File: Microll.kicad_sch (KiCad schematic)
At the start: 13 parts, among them J1 USB_C_Receptacle, U1 AP7173-FNG-7, U2 STM32G0B1CBU6, U3 ESP32-C3-WROOM-02-N4, U4 LSM6DSL

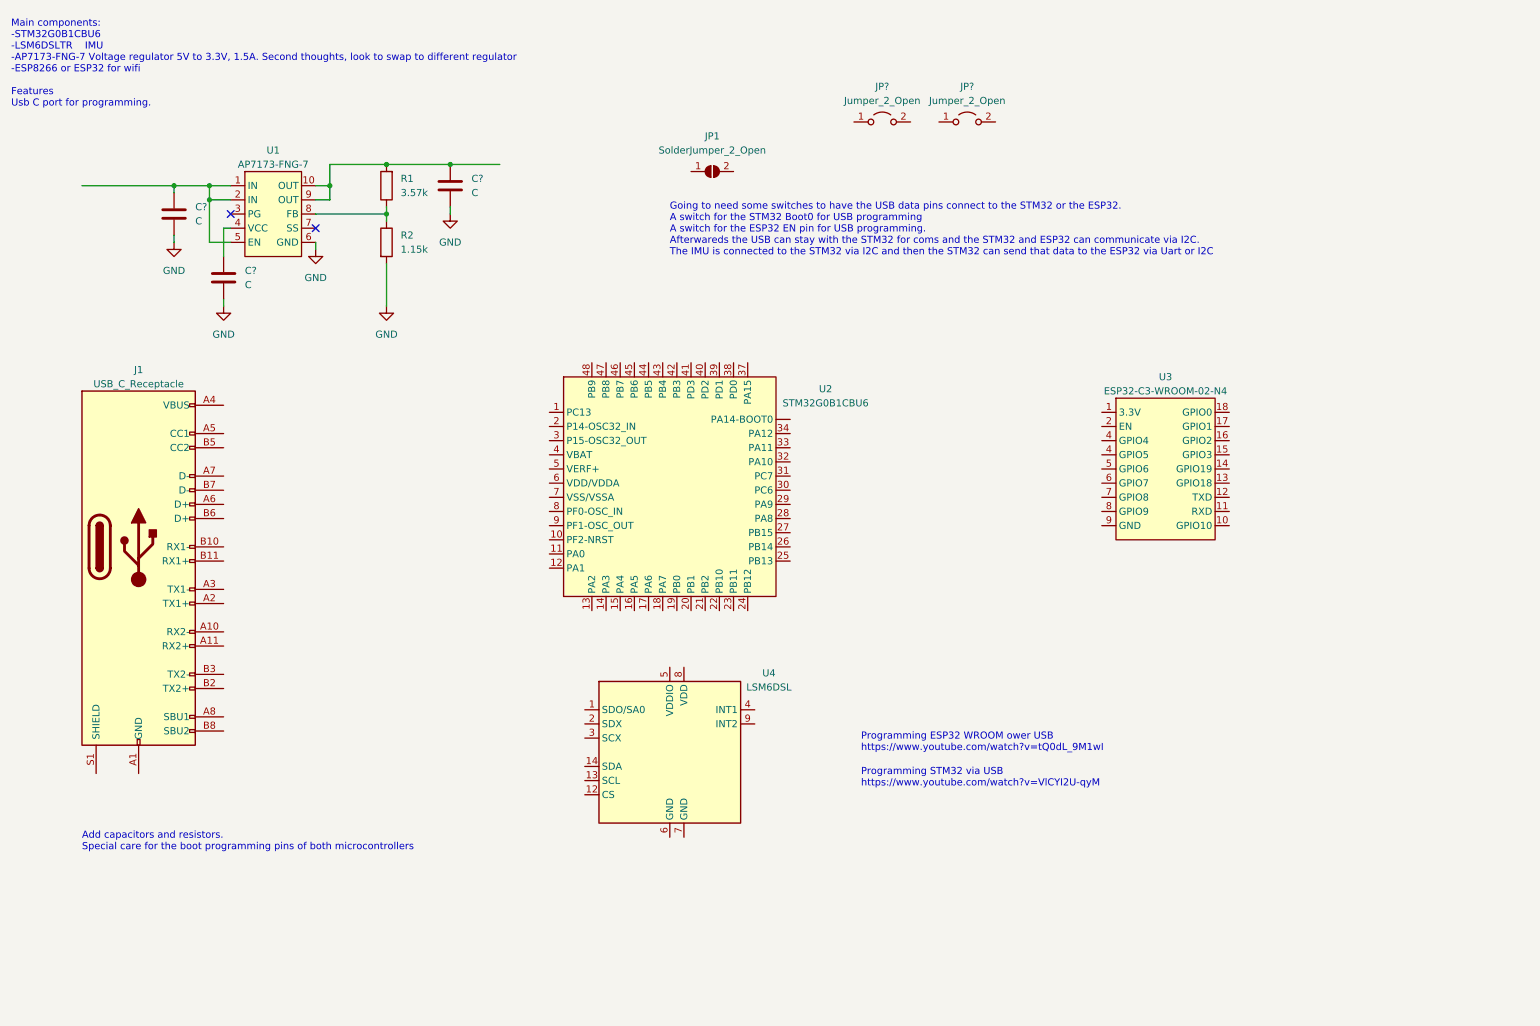
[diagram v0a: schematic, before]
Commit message: Changed linear regulator to TLV767
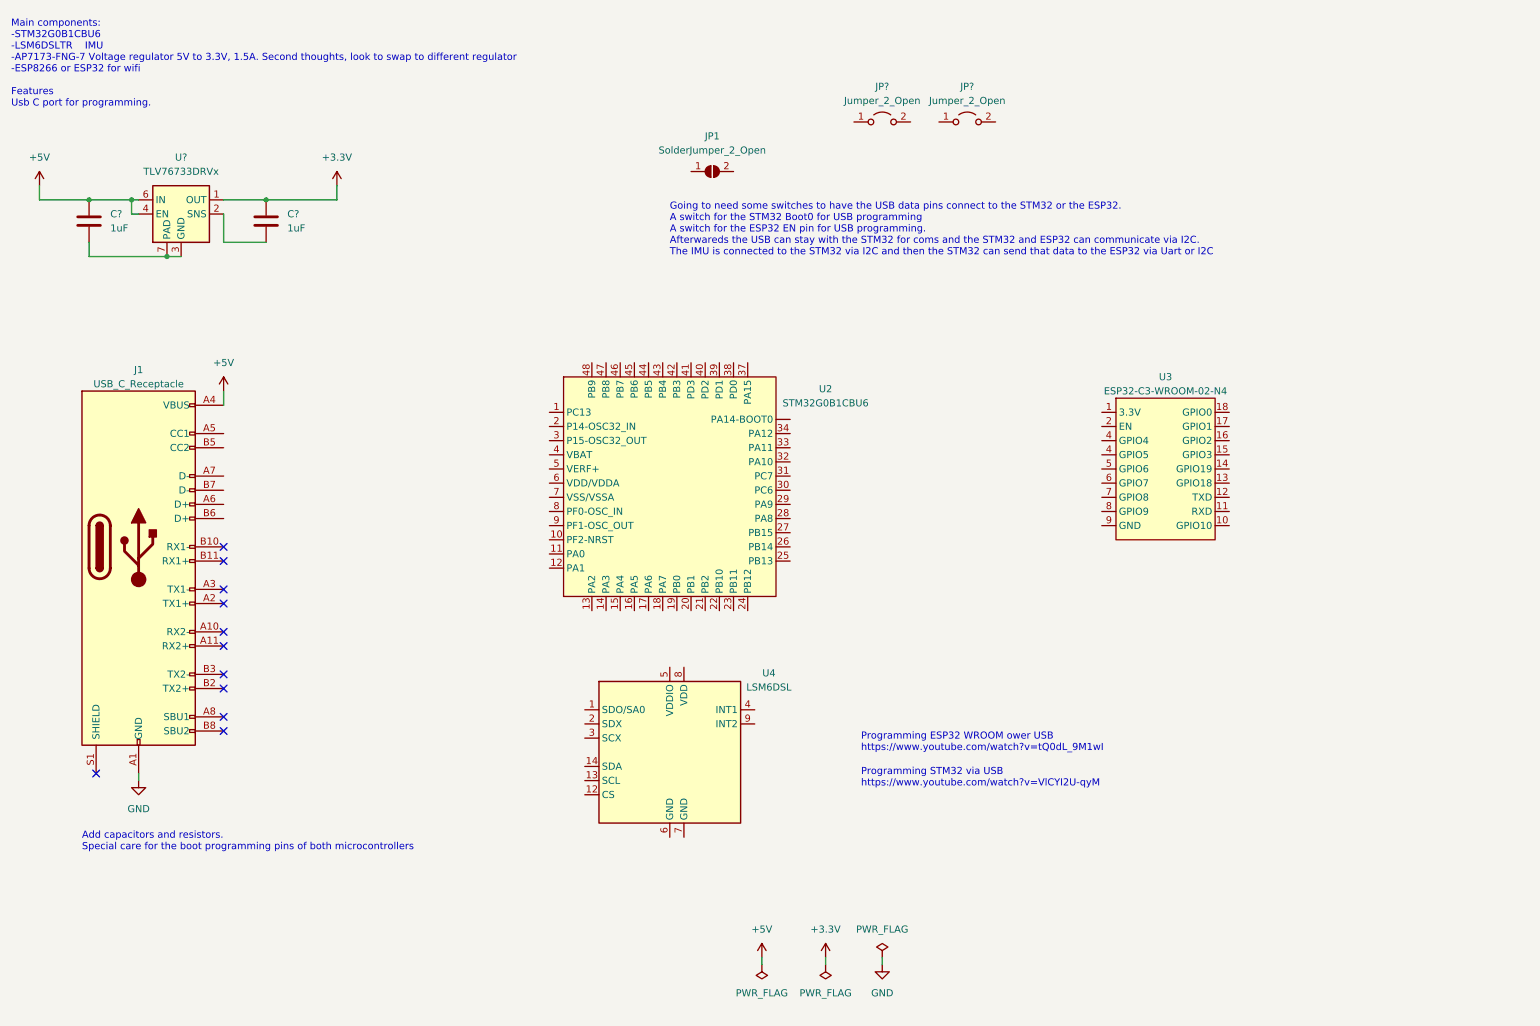
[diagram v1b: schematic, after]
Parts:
- removed C? (x3): C, symbol Device:C
- removed R1: 3.57k, symbol Device:R
- removed R2: 1.15k, symbol Device:R
- removed U1: AP7173-FNG-7, AP7173-FNG-7:AP7173-FNG-7, symbol AP7173-FNG-7:AP7173-FNG-7
- added C? (x2): 1uF, symbol Device:C
- added U?: TLV76733DRVx, Package_SON:WSON-6-1EP_2x2mm_P0.65mm_EP1x1.6mm_ThermalVias, symbol Regulator_Linear:TLV76733DRVx
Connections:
- net GND: now also J1.A1 (GND), J1.A12 (GND), J1.B1 (GND), J1.B12 (GND)
- net +5V: now reaches J1.A4 (VBUS), J1.A9 (VBUS), J1.B4 (VBUS), J1.B9 (VBUS)
- net +5V: now also C?.1, U?.4 (EN), U?.6 (IN)
- new net: C?.2, U?.2 (SNS)
- new net: C?.2, U?.3 (GND), U?.5 (GND), U?.7 (PAD)
- new net +3.3V: C?.1, U?.1 (OUT)
- no-connect marks 2 -> 11
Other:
- title: (none) -> Microll

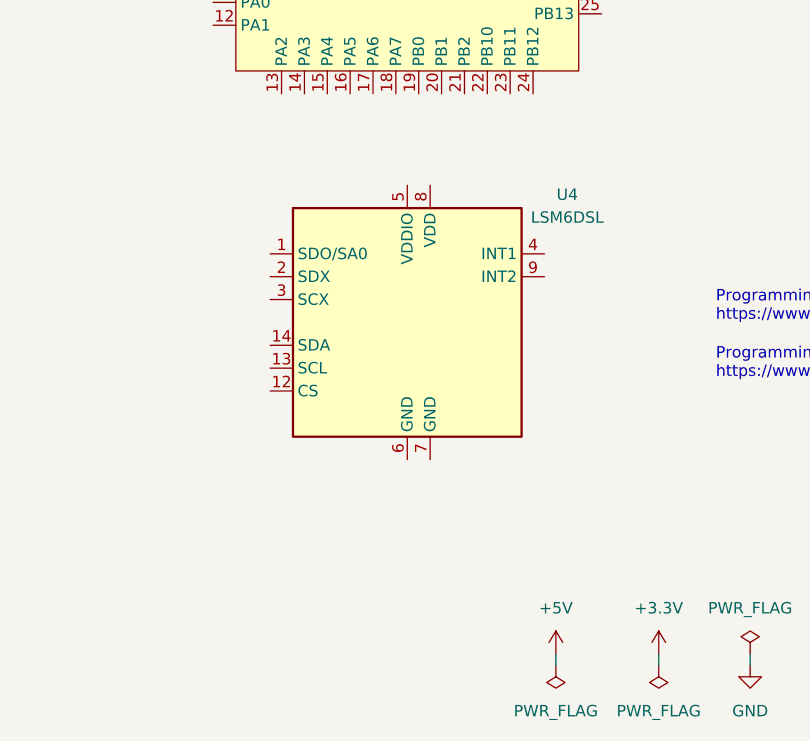
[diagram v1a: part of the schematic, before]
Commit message: added some capacitors to the IMU
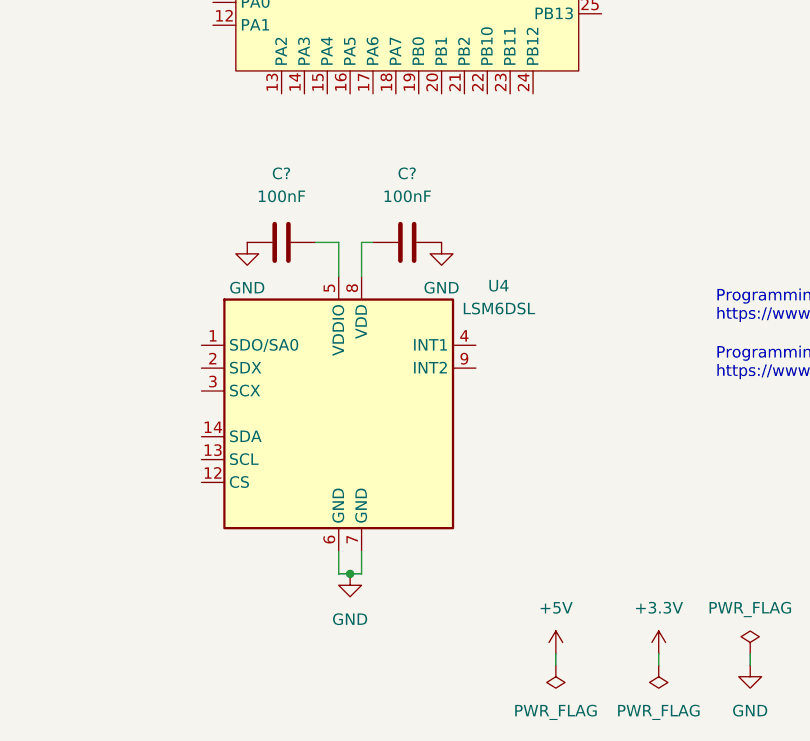
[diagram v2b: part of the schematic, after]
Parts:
- added C? (x2): 100nF, symbol Device:C
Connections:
- net GND: now also U4.6 (GND), U4.7 (GND), C?.2, C?.2
- net at U4.5 (VDDIO): now also C?.1
- net at U4.8 (VDD): now also C?.1
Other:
- moved on the sheet: U4
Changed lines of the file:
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@@
   (junction (at 36.83 48.26) (diameter 0) (color 0 0 0 0)
+  )
+  (junction (at 127 175.26) (diameter 0) (color 0 0 0 0)
   )
   (junction (at 60.96 48.26) (diameter 0) (color 0 0 0 0)
@@
     (stroke (width 0) (type default) (color 0 0 0 0))
   )
+  (wire (pts (xy 123.19 138.43) (xy 125.73 138.43))
+    (stroke (width 0) (type default) (color 0 0 0 0))
+  )
   (wire (pts (xy 60.96 48.26) (xy 73.66 48.26))
     (stroke (width 0) (type default) (color 0 0 0 0))
@@
     (stroke (width 0) (type default) (color 0 0 0 0))
   )
+  (wire (pts (xy 125.73 172.72) (xy 125.73 175.26))
+    (stroke (width 0) (type default) (color 0 0 0 0))
+  )
+  (wire (pts (xy 128.27 172.72) (xy 128.27 175.26))
+    (stroke (width 0) (type default) (color 0 0 0 0))
+  )
+  (wire (pts (xy 125.73 138.43) (xy 125.73 142.24))
+    (stroke (width 0) (type default) (color 0 0 0 0))
+  )
   (wire (pts (xy 171.45 184.15) (xy 171.45 185.42))
     (stroke (width 0) (type default) (color 0 0 0 0))
   )
+  (wire (pts (xy 128.27 138.43) (xy 129.54 138.43))
+    (stroke (width 0) (type default) (color 0 0 0 0))
+  )
   (wire (pts (xy 38.1 152.4) (xy 38.1 151.13))
     (stroke (width 0) (type default) (color 0 0 0 0))
   )
+  (wire (pts (xy 128.27 142.24) (xy 128.27 138.43))
+    (stroke (width 0) (type default) (color 0 0 0 0))
+  )
   (wire (pts (xy 29.21 48.26) (xy 36.83 48.26))
     (stroke (width 0) (type default) (color 0 0 0 0))
@@
     (stroke (width 0) (type default) (color 0 0 0 0))
   )
+  (wire (pts (xy 125.73 175.26) (xy 127 175.26))
+    (stroke (width 0) (type default) (color 0 0 0 0))
+  )
   (wire (pts (xy 73.66 45.72) (xy 73.66 48.26))
     (stroke (width 0) (type default) (color 0 0 0 0))
   )
   (wire (pts (xy 29.21 58.42) (xy 29.21 55.88))
+    (stroke (width 0) (type default) (color 0 0 0 0))
+  )
+  (wire (pts (xy 128.27 175.26) (xy 127 175.26))
     (stroke (width 0) (type default) (color 0 0 0 0))
   )
@@
     (pin "1")
   )
+  (symbol (lib_id "power:GND") (at 127 175.26 0) (unit 1)
+    (in_bom yes) (on_board yes) (fields_autoplaced)
+    (property "Reference" "#PWR?" (id 0) (at 127 181.61 0)
+      (effects (font (size 1.27 1.27)) hide)
+    )
+    (property "Value" "GND" (id 1) (at 127 180.34 0))
+    (property "Footprint" "" (id 2) (at 127 175.26 0)
+      (effects (font (size 1.27 1.27)) hide)
+    )
+    (property "Datasheet" "" (id 3) (at 127 175.26 0)
+      (effects (font (size 1.27 1.27)) hide)
+    )
+    (pin "1")
+  )
   (symbol (lib_id "power:PWR_FLAG") (at 149.86 185.42 180) (unit 1)
     (in_bom yes) (on_board yes) (fields_autoplaced)
@@
     )
     (property "Datasheet" "" (id 3) (at 20.32 45.72 0)
+      (effects (font (size 1.27 1.27)) hide)
+    )
+    (pin "1")
+  )
+  (symbol (lib_id "power:GND") (at 115.57 138.43 0) (unit 1)
+    (in_bom yes) (on_board yes) (fields_autoplaced)
+    (property "Reference" "#PWR?" (id 0) (at 115.57 144.78 0)
+      (effects (font (size 1.27 1.27)) hide)
+    )
+    (property "Value" "GND" (id 1) (at 115.57 143.51 0))
+    (property "Footprint" "" (id 2) (at 115.57 138.43 0)
+      (effects (font (size 1.27 1.27)) hide)
+    )
+    (property "Datasheet" "" (id 3) (at 115.57 138.43 0)
       (effects (font (size 1.27 1.27)) hide)
     )
@@
     (pin "2")
   )
-  (symbol (lib_id "Sensor_Motion:LSM6DSL") (at 133.35 147.32 0) (unit 1)
-    (in_bom yes) (on_board yes) (fields_autoplaced)
-    (property "Reference" "U4" (id 0) (at 151.13 133.1212 0))
-    (property "Value" "LSM6DSL" (id 1) (at 151.13 135.6612 0))
-    (property "Footprint" "Package_LGA:LGA-14_3x2.5mm_P0.5mm_LayoutBorder3x4y" (id 2) (at 123.19 165.1 0)
+  (symbol (lib_id "Sensor_Motion:LSM6DSL") (at 125.73 157.48 0) (unit 1)
+    (in_bom yes) (on_board yes) (fields_autoplaced)
+    (property "Reference" "U4" (id 0) (at 143.51 143.2812 0))
+    (property "Value" "LSM6DSL" (id 1) (at 143.51 145.8212 0))
+    (property "Footprint" "Package_LGA:LGA-14_3x2.5mm_P0.5mm_LayoutBorder3x4y" (id 2) (at 115.57 175.26 0)
       (effects (font (size 1.27 1.27)) (justify left) hide)
     )
-    (property "Datasheet" "https://www.st.com/resource/en/datasheet/lsm6dsl.pdf" (id 3) (at 135.89 163.83 0)
+    (property "Datasheet" "https://www.st.com/resource/en/datasheet/lsm6dsl.pdf" (id 3) (at 128.27 173.99 0)
       (effects (font (size 1.27 1.27)) hide)
     )
@@
     (pin "1")
   )
+  (symbol (lib_id "Device:C") (at 119.38 138.43 270) (unit 1)
+    (in_bom yes) (on_board yes) (fields_autoplaced)
+    (property "Reference" "C?" (id 0) (at 119.38 130.81 90))
+    (property "Value" "100nF" (id 1) (at 119.38 133.35 90))
+    (property "Footprint" "" (id 2) (at 115.57 139.3952 0)
+      (effects (font (size 1.27 1.27)) hide)
+    )
+    (property "Datasheet" "~" (id 3) (at 119.38 138.43 0)
+      (effects (font (size 1.27 1.27)) hide)
+    )
+    (pin "1")
+    (pin "2")
+  )
+  (symbol (lib_id "power:GND") (at 137.16 138.43 0) (unit 1)
+    (in_bom yes) (on_board yes) (fields_autoplaced)
+    (property "Reference" "#PWR?" (id 0) (at 137.16 144.78 0)
+      (effects (font (size 1.27 1.27)) hide)
+    )
+    (property "Value" "GND" (id 1) (at 137.16 143.51 0))
+    (property "Footprint" "" (id 2) (at 137.16 138.43 0)
+      (effects (font (size 1.27 1.27)) hide)
+    )
+    (property "Datasheet" "" (id 3) (at 137.16 138.43 0)
+      (effects (font (size 1.27 1.27)) hide)
+    )
+    (pin "1")
+  )
+  (symbol (lib_id "Device:C") (at 133.35 138.43 90) (unit 1)
+    (in_bom yes) (on_board yes) (fields_autoplaced)
+    (property "Reference" "C?" (id 0) (at 133.35 130.81 90))
+    (property "Value" "100nF" (id 1) (at 133.35 133.35 90))
+    (property "Footprint" "" (id 2) (at 137.16 137.4648 0)
+      (effects (font (size 1.27 1.27)) hide)
+    )
+    (property "Datasheet" "~" (id 3) (at 133.35 138.43 0)
+      (effects (font (size 1.27 1.27)) hide)
+    )
+    (pin "1")
+    (pin "2")
+  )
   (symbol (lib_id "power:GND") (at 171.45 185.42 0) (unit 1)
     (in_bom yes) (on_board yes) (fields_autoplaced)
@@
       (reference "#PWR?") (unit 1) (value "+5V") (footprint "")
     )
+    (path "/0cdfc0a7-3e48-457a-a8be-7333b8910e5e"
+      (reference "#PWR?") (unit 1) (value "GND") (footprint "")
+    )
     (path "/1a70a061-df21-439a-9d89-e9e6255b7cc1"
       (reference "#PWR?") (unit 1) (value "+5V") (footprint "")
     )
+    (path "/1ab6e6d9-ad66-4da8-933c-ad5c38d4f02c"
+      (reference "#PWR?") (unit 1) (value "GND") (footprint "")
+    )
     (path "/64ad770d-6d13-46f6-8419-84414b81d932"
       (reference "#PWR?") (unit 1) (value "+3.3V") (footprint "")
@@
       (reference "#PWR?") (unit 1) (value "+3.3V") (footprint "")
     )
+    (path "/c072336a-56ed-41bb-9853-ee08efe1ccea"
+      (reference "#PWR?") (unit 1) (value "GND") (footprint "")
+    )
     (path "/dc2a62b9-7cb3-4482-b183-a97abed8b0ea"
       (reference "#PWR?") (unit 1) (value "GND") (footprint "")
@@
       (reference "C?") (unit 1) (value "1uF") (footprint "")
     )
+    (path "/a8a78770-0fd0-4108-aaf8-5dba8c7b4384"
+      (reference "C?") (unit 1) (value "100nF") (footprint "")
+    )
+    (path "/cee9ab8e-62c7-4eeb-b82f-bf642973fbd3"
+      (reference "C?") (unit 1) (value "100nF") (footprint "")
+    )
     (path "/9dc9595c-915c-4807-bd39-25a9004629d5"
